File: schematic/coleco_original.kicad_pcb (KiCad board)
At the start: 2 copper layers, 88.7 x 116.7 mm, 62 parts, among them J1 Barrel_Jack_Switch, J2 Conn_01x02, J3 Conn_Coaxial, J4 Cartridge Port, J5 Player 1, J6 Conn_02x05_Odd_Even, J7 Player 2, J8 Conn_01x03, Q1 2N3904, SW1 SW_Push, U1 LM386, U2 SN76489AN, U3 Z84C0010AEG, U4 6116XA, U5 AT27C256R-70JU-T, U6 TMS9118NL, U7 TMS4416, U8 TMS4416, U9 EPM7064SLC, Y1 Crystal

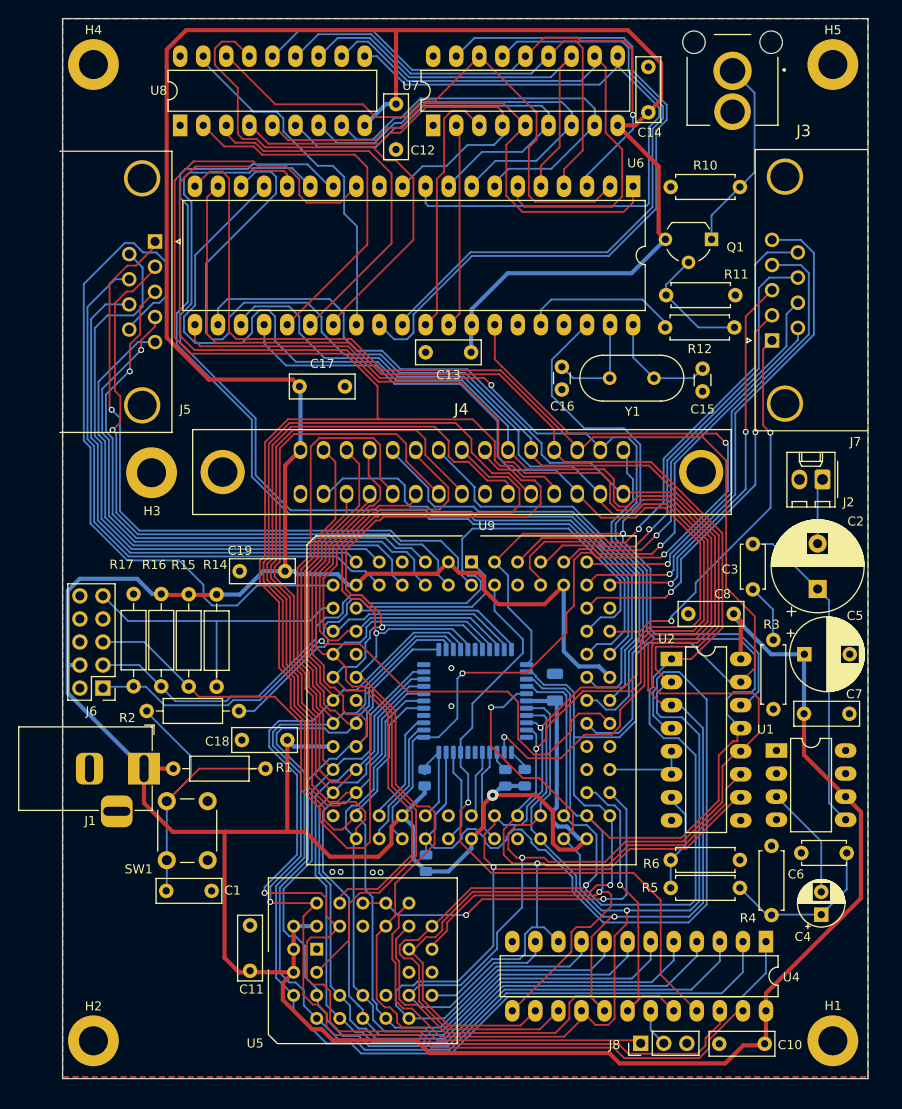
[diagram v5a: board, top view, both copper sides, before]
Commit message: moved JTAG connector over to make room for power on side of board
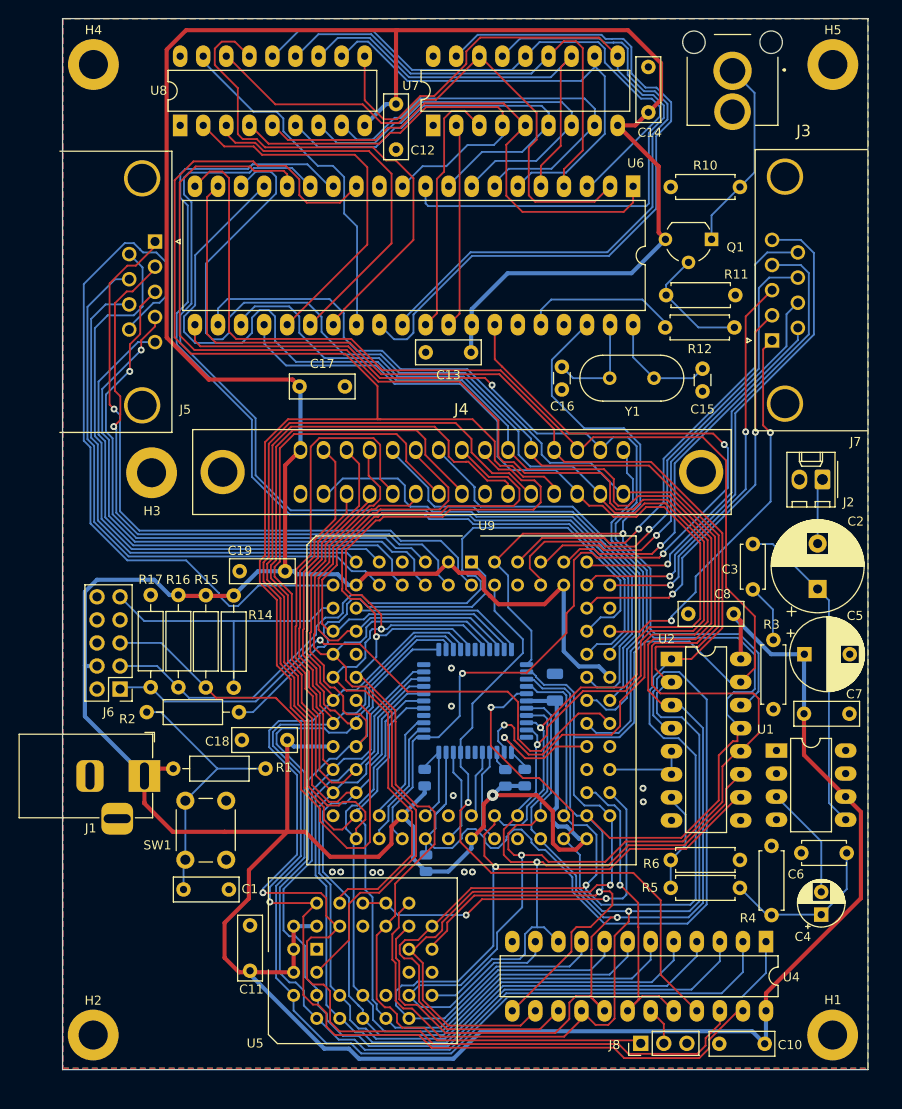
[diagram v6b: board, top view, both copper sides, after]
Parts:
- moved SW1 2.04 mm to (95.4, 148.1)
- moved C1 1.91 mm to (95.2, 151.3)
- moved J6 1.89 mm to (88.2, 129.3)
- moved R14 1.89 mm to (100.8, 129.1)
- moved R16 1.89 mm to (94.7, 129.1)
- moved R15 1.89 mm to (97.7, 129.1)
- moved R17 1.89 mm to (91.6, 129.1)
- moved J1 0.81 mm to (90.9, 138.8)
- moved H1 0.64 mm to (166.7, 167.4)
- moved H2 0.64 mm to (85.3, 167.4)
- moved R2 0.13 mm to (91.2, 131.8)
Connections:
- R9 pad 1: /cpu/~{INT} -> /GLUE/~{INT}
- U3 pad 12: /cpu/~{INT} -> /GLUE/~{INT}
- U9 pad 60: /GLUE/RX -> unconnected-(U9-I/O-Pad60)
- U9 pad 61: /GLUE/TX -> /GLUE/~{INT}
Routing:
- net /GLUE/~{INT}: track 0.00 -> 15.0 mm, vias 0 -> 1
- net /video/AD0: track 74.1 -> 85.4 mm
- net /video/AD4: track 62.6 -> 53.1 mm
- net Net-(C1-Pad1): track 35.4 -> 30.7 mm
- net /GLUE/TCK: track 70.2 -> 67.0 mm
- net +5V: track 570.2 -> 573.3 mm
- net /cpu/~{NMI}: track 147.4 -> 150.2 mm
- net /cpu/~{INT}: track 2.48 -> 0.00 mm
- net /GLUE/TDO: track 85.6 -> 83.1 mm
- net /GLUE/TMS: track 60.4 -> 58.5 mm
- net /GLUE/TDI: track 34.0 -> 32.3 mm
- net /video/R3: track 78.8 -> 80.1 mm
- net /video/R2: track 67.6 -> 68.9 mm
- net /video/AD7: track 61.7 -> 63.0 mm, vias 1 -> 0
- net /GLUE/D1: track 177.0 -> 176.1 mm
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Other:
- board size 88.7 x 116.7 mm -> 88.7 x 115.7 mm
